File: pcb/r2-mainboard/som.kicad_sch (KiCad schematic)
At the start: 14 parts, among them J21 MICRO_SD(TFC-WPAPR-08), J26 BTH-060-01-L-D-A-K-TR, J27 BTH-060-01-L-D-A-K-TR, X2 PCM-071

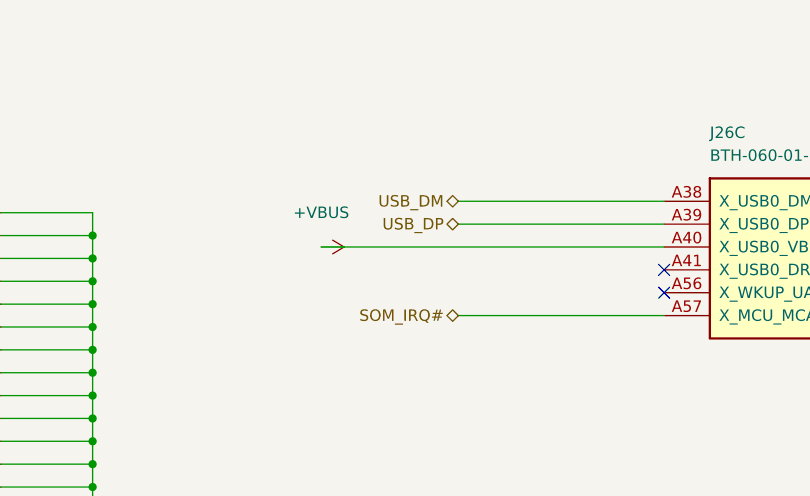
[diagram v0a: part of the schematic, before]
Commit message: R2: withdraw the RWU0007A thermal-pad concern -- it was wrong
power.md §7 item 2 said KiCad's Texas_RWU0007A_VQFN-7_2x2mm_P0.5mm leaves the
thermal-pad segments unnumbered, so U12's heat path is not tied to GND, and to
copy the footprint into r2.pretty and renumber those pads 1 before layout.

Reading the placed footprint with the layer field visible: the six unnumbered
pads are F.Paste ONLY. They are stencil apertures -- each large pad split into
two openings to control solder volume, the standard idiom at that size. Pads
1/2/3 are F.Cu + F.Mask, numbered, and netted GND / SW / +5V_DCDC. Pin 1 is the
thermal path per Table 5-1 and it is on GND already.

Acting on the note would have renumbered paste apertures into copper and
shorted GND, SW and VOUT together -- creating the failure it was meant to
prevent. Found because the owner is routing U12 right now.

§11.2 item 5 amended to a plain layout instruction, and §8's open-items list
no longer carries it.

Co-Authored-By: Claude Opus 5 <noreply@anthropic.com>
Claude-Session: https://claude.ai/code/session_01MnesETWABbVdbcVnCKfKVs
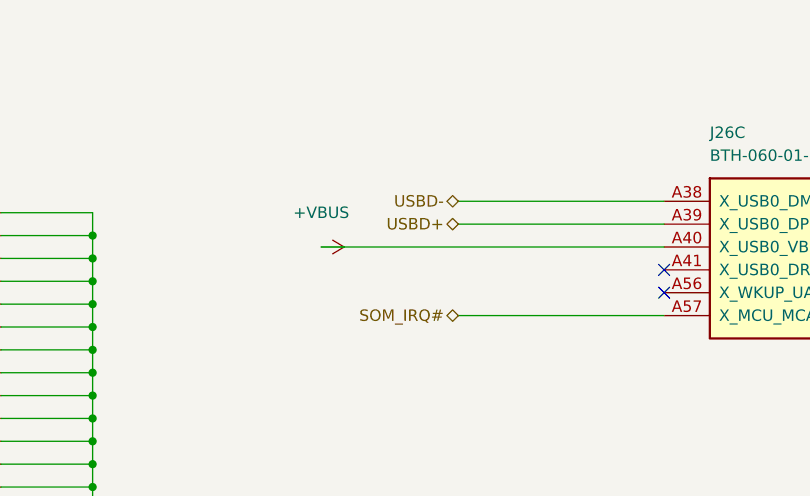
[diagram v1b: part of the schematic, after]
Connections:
- net USB_DM renamed USBD-
- net USB_DP renamed USBD+
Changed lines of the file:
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@@
 		)
 	)
-	(hierarchical_label "USB_DP"
+	(hierarchical_label "USBD+"
 		(shape bidirectional)
 		(at 154.94 40.64 180)
@@
 		)
 	)
-	(hierarchical_label "USB_DM"
+	(hierarchical_label "USBD-"
 		(shape bidirectional)
 		(at 154.94 38.1 180)
